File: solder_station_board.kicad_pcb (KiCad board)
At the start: 2 copper layers, 104.8 x 60.3 mm, 34 parts, among them J1 Conn_01x04, J2 Conn_FB, J3 RT_WELLER, J4 VFD dISPLAY, J6 PWR_15V, P1 ISP, Q1 IRF9540, Q2 2N7002, U4 TLC272, U5 LT1007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

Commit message: Add inputs and refine
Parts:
- added J5: INPUT, Connector_PinSocket_2.54mm:PinSocket_1x03_P2.54mm_Vertical, F.Cu at (48.1, 68.0)
- added J7: INT_PWR, Connector_PinHeader_2.54mm:PinHeader_2x02_P2.54mm_Vertical, F.Cu at (50.4, 55.8)
- added J8: SERIAL, Connector_PinHeader_2.54mm:PinHeader_1x03_P2.54mm_Vertical, F.Cu at (48.1, 77.9)
- added R1: 1k, Resistor_SMD:R_0805_2012Metric_Pad1.15x1.40mm_HandSolder, B.Cu at (52.4, 62.9)
- added R2: 1k, Resistor_SMD:R_0805_2012Metric_Pad1.15x1.40mm_HandSolder, B.Cu at (57.6, 62.9)
- added R3: 1k, Resistor_SMD:R_0805_2012Metric_Pad1.15x1.40mm_HandSolder, B.Cu at (55.0, 62.9)
- J1: value Conn_01x04 -> PWR_5_36
- R10, R15, R5: footprint Resistor_SMD:R_0805_2012Metric_Pad1.15x1.40mm_HandSolder -> Resistor_SMD:R_1206_3216Metric_Pad1.42x1.75mm_HandSolder
- moved J3 69.6 mm to (115.0, 36.7), turned to 90 degrees
- moved C7 68.7 mm to (118.7, 46.8), turned to 270 degrees
- moved R7 66.3 mm to (116.2, 46.8), turned to 90 degrees
- moved R5 63.5 mm to (113.4, 43.6), turned to 90 degrees
- moved U5 49.8 mm to (107.8, 45.9), turned to 270 degrees
- moved R10 40.9 mm to (105.9, 39.8), turned to 180 degrees
- moved U7 34.3 mm to (120.2, 67.1), turned to 0 degrees
- moved R12 32.5 mm to (100.5, 40.0), turned to 180 degrees
- moved J1 32.2 mm to (47.8, 42.7), turned to 0 degrees
- moved R9 28.4 mm to (124.7, 54.0)
- moved Q2 28.1 mm to (130.3, 54.5)
- moved U4 27.7 mm to (101.4, 45.9), turned to 270 degrees
- moved R8 26.7 mm to (124.7, 51.0), turned to 0 degrees
- moved R13 23.8 mm to (96.5, 41.0), turned to 270 degrees
- moved R6 23.1 mm to (139.4, 42.8), turned to 0 degrees
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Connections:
- J4 pad 21: /f -> /b
- J4 pad 22: /e -> /1G
- J4 pad 23: /2G -> /a
- J4 pad 24: /d -> /S12
- J4 pad 25: /c -> /S10
- J4 pad 27: /b -> /c
- J4 pad 28: /a -> /d
- J4 pad 29: /S12 -> /2G
- J4 pad 30: /1G -> /e
- J4 pad 32: /S10 -> /f
- U6 pad 1: (no net) -> /INP2
- U6 pad 2: (no net) -> /INP3
- U6 pad 24: /SDI -> /CLOCK
- U6 pad 25: /CLOCK -> /STROBE
- U6 pad 26: /STROBE -> /BLANK
- U6 pad 27: /BLANK -> /SDI
- U6 pad 30: (no net) -> Net-(J8-Pad1)
- U6 pad 31: (no net) -> Net-(J8-Pad2)
- U6 pad 32: (no net) -> /INP1
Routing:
- net Net-(J3-Pad2): track 131.3 -> 31.6 mm
- net /SDI: track 25.4 -> 72.2 mm, vias 0 -> 2
- net -5V: track 35.2 -> 80.0 mm
- net +36V: track 60.5 -> 104.6 mm, vias 2 -> 4
- net /CLOCK: track 9.96 -> 53.9 mm
- net /STROBE: track 14.3 -> 55.2 mm
- net /S8: track 27.1 -> 65.7 mm
- net /7G: track 25.8 -> 62.4 mm
- net GND: track 26.0 -> 62.5 mm, vias 0 -> 2
- net /S7: track 23.9 -> 59.5 mm
- net /S10: track 52.1 -> 18.1 mm
- net /INP1: track 0.00 -> 34.0 mm
- net /6G: track 20.6 -> 53.7 mm
- net /S5: track 19.7 -> 50.6 mm
- net Net-(J8-Pad1): track 0.00 -> 29.9 mm
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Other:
- board size 104.8 x 60.3 mm -> 104.6 x 55.9 mm

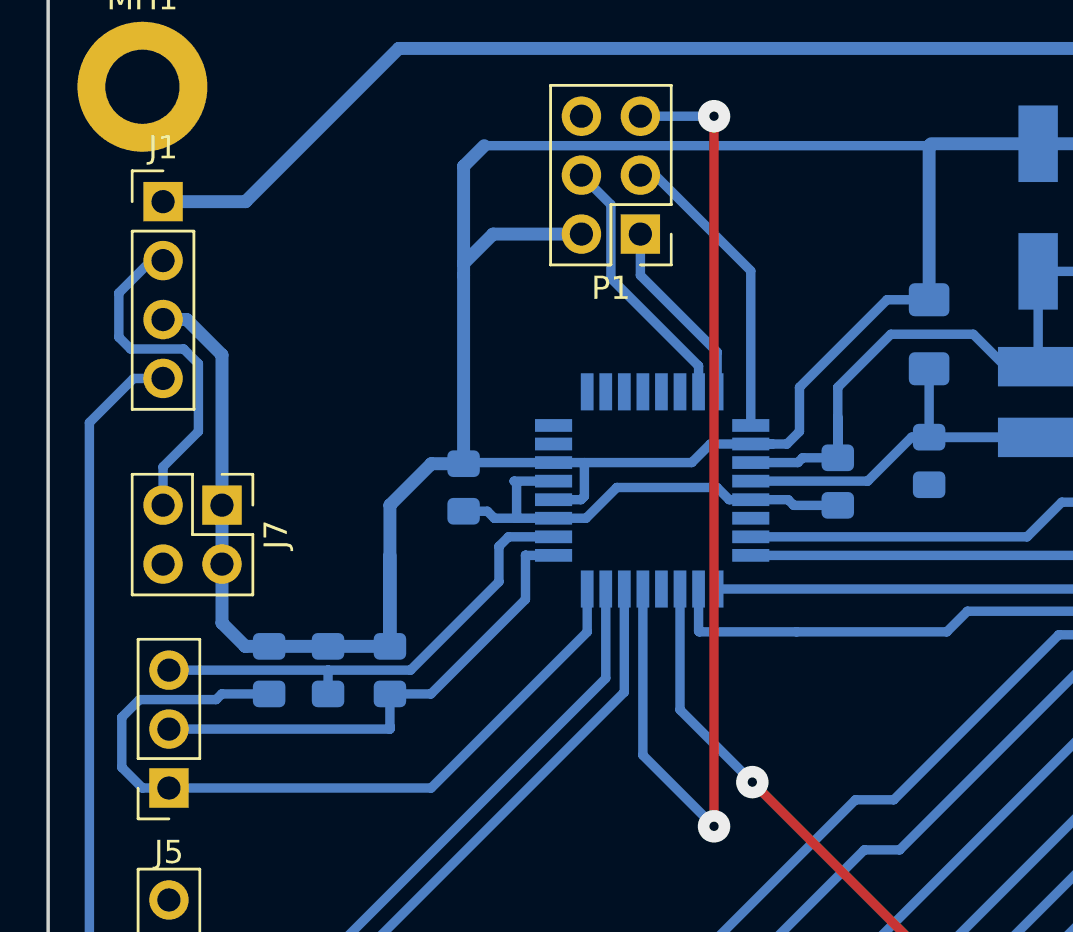
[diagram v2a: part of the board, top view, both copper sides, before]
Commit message: Add more inputs
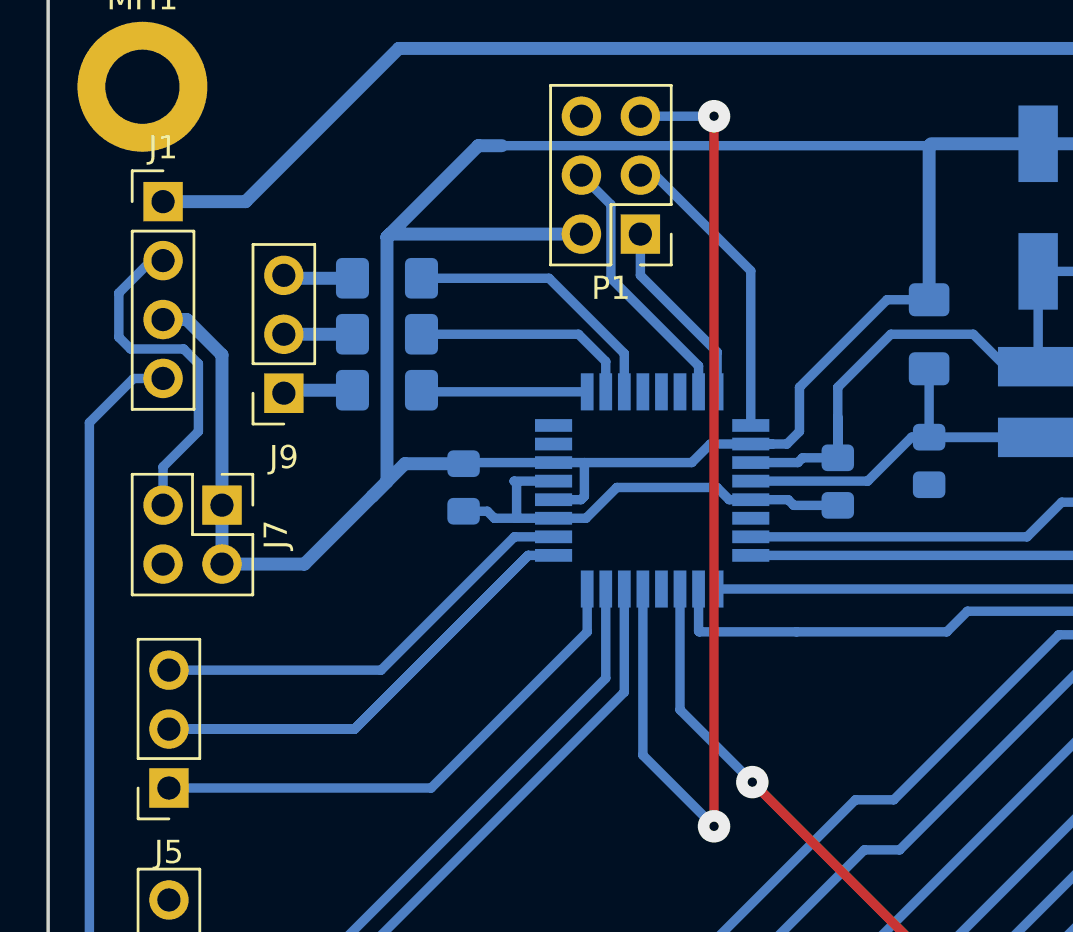
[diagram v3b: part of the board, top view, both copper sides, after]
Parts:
- added J9: INPUT, Connector_PinSocket_2.54mm:PinSocket_1x03_P2.54mm_Vertical, F.Cu at (53.0, 51.0)
- R1, R2, R3: value 1k -> 0; footprint Resistor_SMD:R_0805_2012Metric_Pad1.15x1.40mm_HandSolder -> Resistor_SMD:R_1206_3216Metric_Pad1.42x1.75mm_HandSolder
- moved R3 17.1 mm to (57.5, 46.0), turned to 0 degrees
- moved R2 14.5 mm to (57.5, 48.4), turned to 0 degrees
- moved R1 13.1 mm to (57.5, 50.8), turned to 0 degrees
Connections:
- R1 pad 1: +5V -> Net-(J9-Pad1)
- R1 pad 2: /INP1 -> /INP4
- R2 pad 1: +5V -> Net-(J9-Pad2)
- R2 pad 2: /INP2 -> /INP5
- R3 pad 1: +5V -> Net-(J9-Pad3)
- R3 pad 2: /INP3 -> /INP6
- U6 pad 10: (no net) -> /INP5
- U6 pad 11: (no net) -> /INP6
- U6 pad 9: (no net) -> /INP4
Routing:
- net /INP2: track 21.8 -> 38.3 mm
- net /INP6: track 0.00 -> 11.7 mm
- net /INP1: track 34.0 -> 22.7 mm
- net /INP5: track 0.00 -> 9.74 mm
- net /INP4: track 0.00 -> 7.17 mm
- net +5V: track 187.6 -> 181.1 mm
- net Net-(J9-Pad3): track 0.00 -> 3.01 mm
- net Net-(J9-Pad1): track 0.00 -> 3.01 mm
- net Net-(J9-Pad2): track 0.00 -> 2.96 mm
- net /INP3: track 20.9 -> 19.0 mm

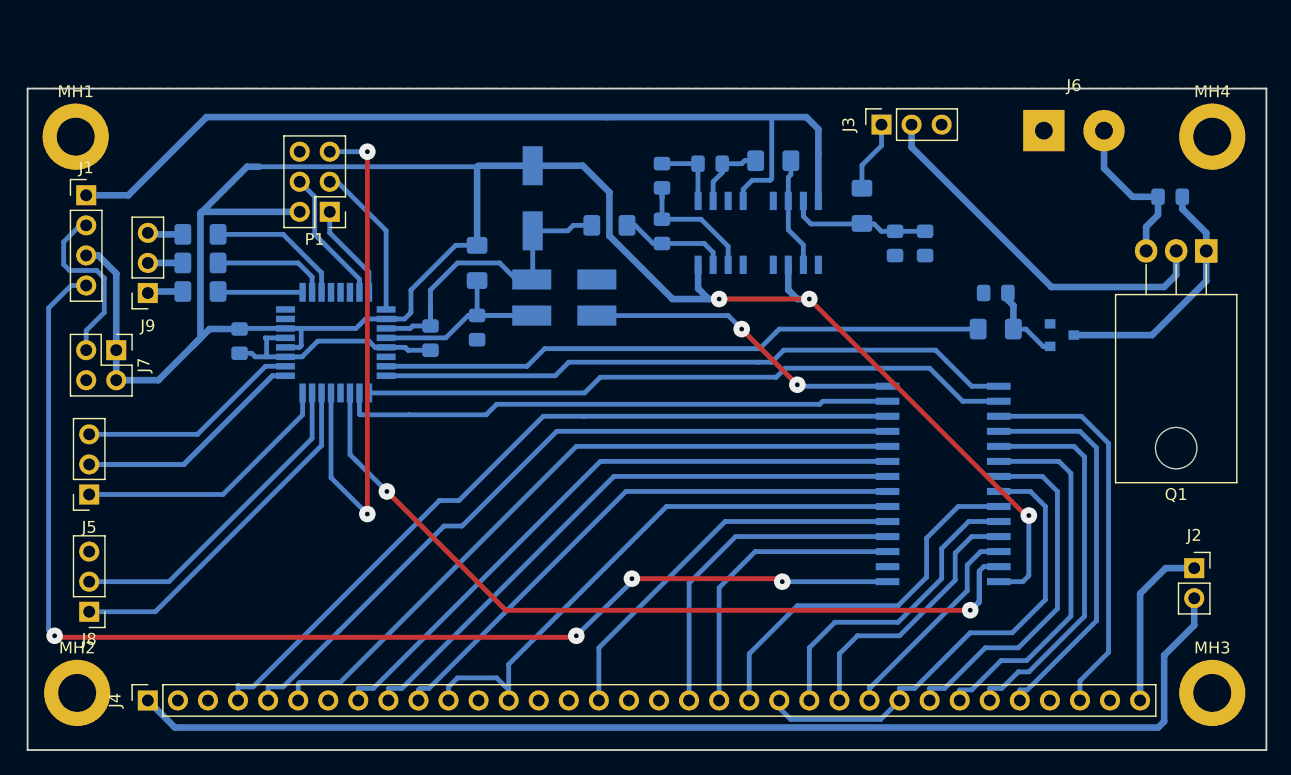
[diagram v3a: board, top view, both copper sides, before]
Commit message: compensate the delta voltage input with resistors
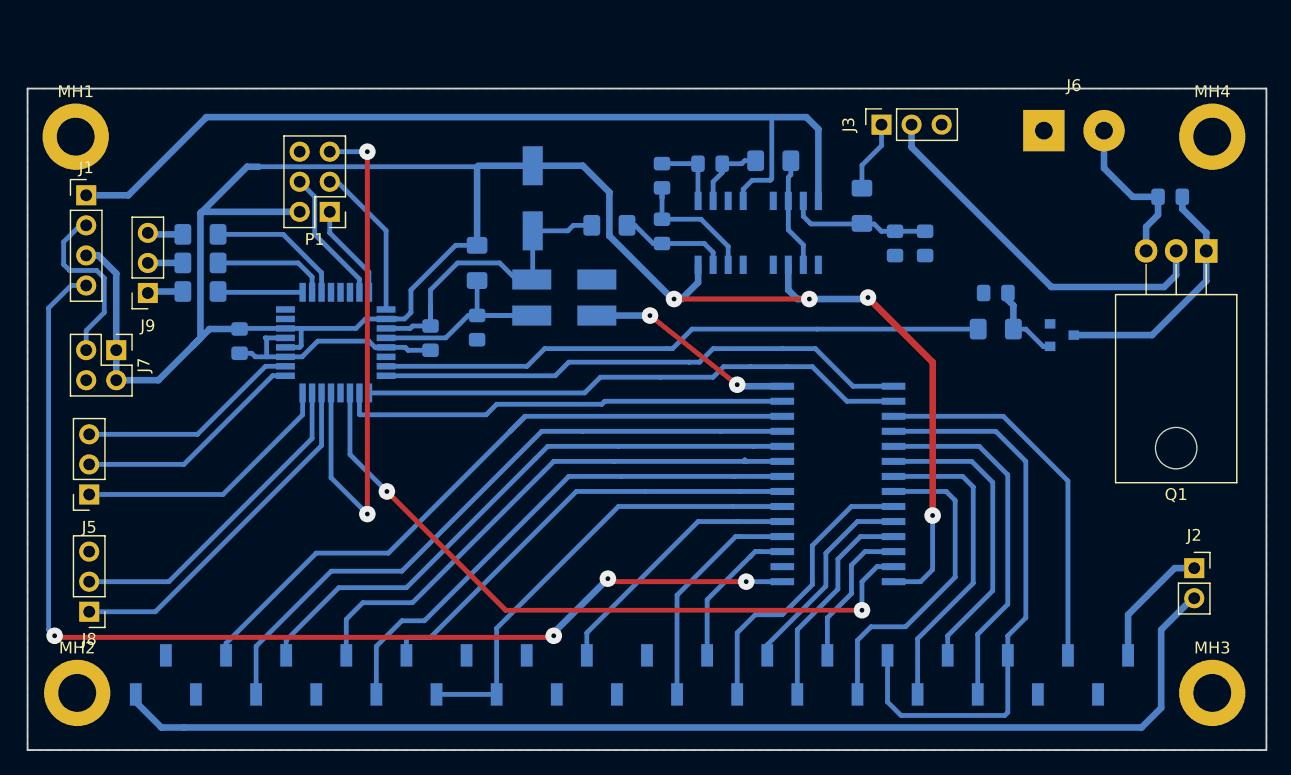
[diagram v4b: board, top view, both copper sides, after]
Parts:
- J4: footprint Connector_PinSocket_2.54mm:PinSocket_1x34_P2.54mm_Vertical -> Connector_PinSocket_2.54mm:PinSocket_1x34_P2.54mm_Vertical_SMD_Pin1Right; moved to B.Cu
- moved J4 41.0 mm to (93.9, 83.2), turned to 270 degrees
- moved U7 8.89 mm to (111.3, 67.1)
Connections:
- J4 pad 21: /b -> /f
- J4 pad 22: /1G -> /e
- J4 pad 23: /a -> /2G
- J4 pad 24: /S12 -> /d
- J4 pad 25: /S10 -> /c
- J4 pad 27: /c -> /b
- J4 pad 28: /d -> /a
- J4 pad 29: /2G -> /S12
- J4 pad 30: /e -> /1G
- J4 pad 32: /f -> /S10
- U7 pad 17: /f -> /S10
- U7 pad 18: /e -> /1G
- U7 pad 19: /2G -> /S12
- U7 pad 20: /d -> /a
- U7 pad 21: /c -> /b
- U7 pad 22: /1G -> /c
- U7 pad 23: /b -> /f
- U7 pad 24: /a -> /e
- U7 pad 25: /S12 -> /2G
- U7 pad 26: /S10 -> /d
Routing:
- net /d: track 31.4 -> 12.5 mm
- net /INP2: track 38.3 -> 19.7 mm
- net /e: track 33.2 -> 17.5 mm
- net /2G: track 32.6 -> 18.3 mm
- net /S10: track 18.1 -> 31.7 mm
- net /SDI: track 72.2 -> 59.5 mm
- net /3G: track 25.1 -> 12.7 mm
- net /4G: track 33.2 -> 22.3 mm
- net /S7: track 59.5 -> 50.0 mm
- net /5G: track 48.4 -> 39.1 mm
- net /S4: track 47.5 -> 38.3 mm
- net /g: track 28.3 -> 19.3 mm
- net +36V: track 104.6 -> 95.7 mm
- net /BLANK: track 46.9 -> 38.0 mm
- net /CLOCK: track 53.9 -> 45.1 mm
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
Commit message: add resistor to the + input of opamp
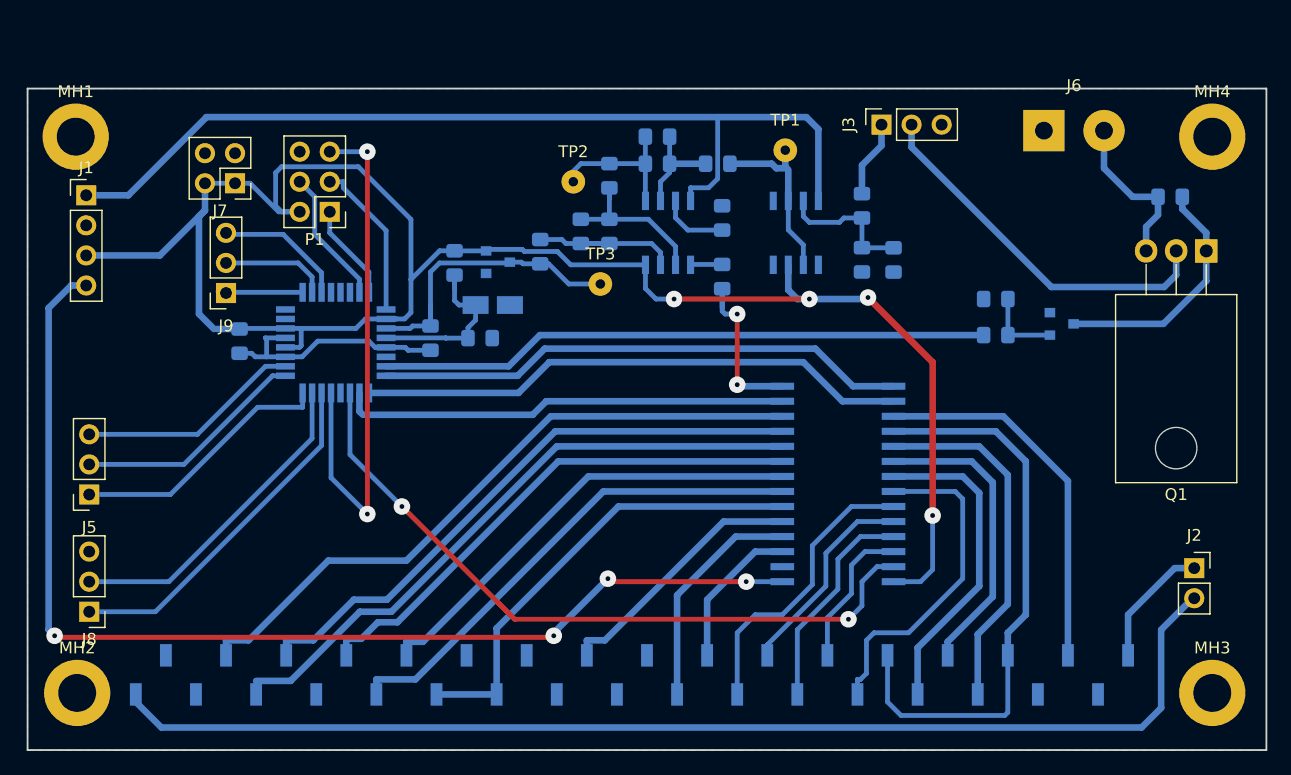
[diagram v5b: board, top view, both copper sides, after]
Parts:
- removed D3, D7: 1N4148, Diode_SMD:D_MiniMELF_Handsoldering
- removed R1, R2, R3: 0, Resistor_SMD:R_1206_3216Metric_Pad1.42x1.75mm_HandSolder
- added C1: 10n, Capacitor_SMD:C_0805_2012Metric_Pad1.15x1.40mm_HandSolder, B.Cu at (96.1, 37.7)
- added C2: 10n, Capacitor_SMD:C_0805_2012Metric_Pad1.15x1.40mm_HandSolder, B.Cu at (89.6, 45.7)
- added D1: BAT54S, Package_TO_SOT_SMD:SOT-23, B.Cu at (82.6, 48.3)
- added R16: 1k, Resistor_SMD:R_0805_2012Metric_Pad1.15x1.40mm_HandSolder, B.Cu at (101.6, 49.6)
- added R4: 1k, Resistor_SMD:R_0805_2012Metric_Pad1.15x1.40mm_HandSolder, B.Cu at (101.6, 44.6)
- added TP1: tp, Connector_Wire:SolderWirePad_1x01_Drill0.8mm, F.Cu at (106.9, 38.9)
- added TP2: tp, Connector_Wire:SolderWirePad_1x01_Drill0.8mm, F.Cu at (89.0, 41.6)
- added TP3: tp, Connector_Wire:SolderWirePad_1x01_Drill0.8mm, F.Cu at (91.3, 50.2)
- D8: footprint Diode_SMD:D_MiniMELF_Handsoldering -> Diode_SMD:D_MicroMELF_Hadsoldering
- R10, R11, R15, R5, R9: footprint Resistor_SMD:R_1206_3216Metric_Pad1.42x1.75mm_HandSolder -> Resistor_SMD:R_0805_2012Metric_Pad1.15x1.40mm_HandSolder
- moved J7 17.3 mm to (60.4, 41.7), turned to 180 degrees
- moved J9 6.60 mm to (59.7, 51.0)
- moved R15 6.25 mm to (86.2, 47.5), turned to 270 degrees
- moved D8 6.11 mm to (82.2, 52.0)
- moved R10 4.70 mm to (101.2, 40.0)
- moved R12 4.45 mm to (96.1, 40.0)
- moved U4 4.45 mm to (97.0, 45.9)
- moved R13 4.44 mm to (92.0, 41.0)
- moved R14 4.44 mm to (92.0, 45.7)
- moved R7 3.12 mm to (113.4, 48.1)
- moved C7 3.01 mm to (116.0, 48.2)
- moved R11 1.91 mm to (79.0, 48.4)
- moved Q2 0.95 mm to (130.2, 53.6)
- moved C8 0.92 mm to (81.1, 54.8), turned to 0 degrees
- moved R9 0.51 mm to (124.7, 54.5)
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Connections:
- J9 pad 1: Net-(J9-Pad1) -> /INP4
- J9 pad 2: Net-(J9-Pad2) -> /INP5
- J9 pad 3: Net-(J9-Pad3) -> /INP6
- U4 pad 3: GND -> Net-(R4-Pad1)
- U4 pad 5: GND -> Net-(R16-Pad1)
- U7 pad 10: /S7 -> /7G
- U7 pad 11: /7G -> /S7
- U7 pad 7: /S4 -> /S5
- U7 pad 8: /S5 -> /S4
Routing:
- net /SOLDER: track 51.3 -> 88.6 mm
- net +5V: track 181.1 -> 161.5 mm
- net GND: track 53.8 -> 36.0 mm
- net /6G: track 45.6 -> 63.2 mm
- net /S5: track 44.3 -> 57.4 mm
- net Net-(C1-Pad2): track 6.19 -> 12.7 mm
- net Net-(R10-Pad1): track 9.41 -> 15.5 mm
- net Net-(R4-Pad1): track 0.00 -> 5.80 mm
- net Net-(C8-Pad1): track 20.3 -> 15.2 mm
- net Net-(C2-Pad2): track 9.27 -> 14.1 mm
- net Net-(J9-Pad3): track 3.01 -> 0.00 mm
- net Net-(J9-Pad1): track 3.01 -> 0.00 mm
- net Net-(J9-Pad2): track 2.96 -> 0.00 mm
- net Net-(R16-Pad1): track 0.00 -> 2.68 mm
- net /TEMP: track 28.2 -> 25.6 mm
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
